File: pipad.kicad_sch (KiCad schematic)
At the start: 2 parts

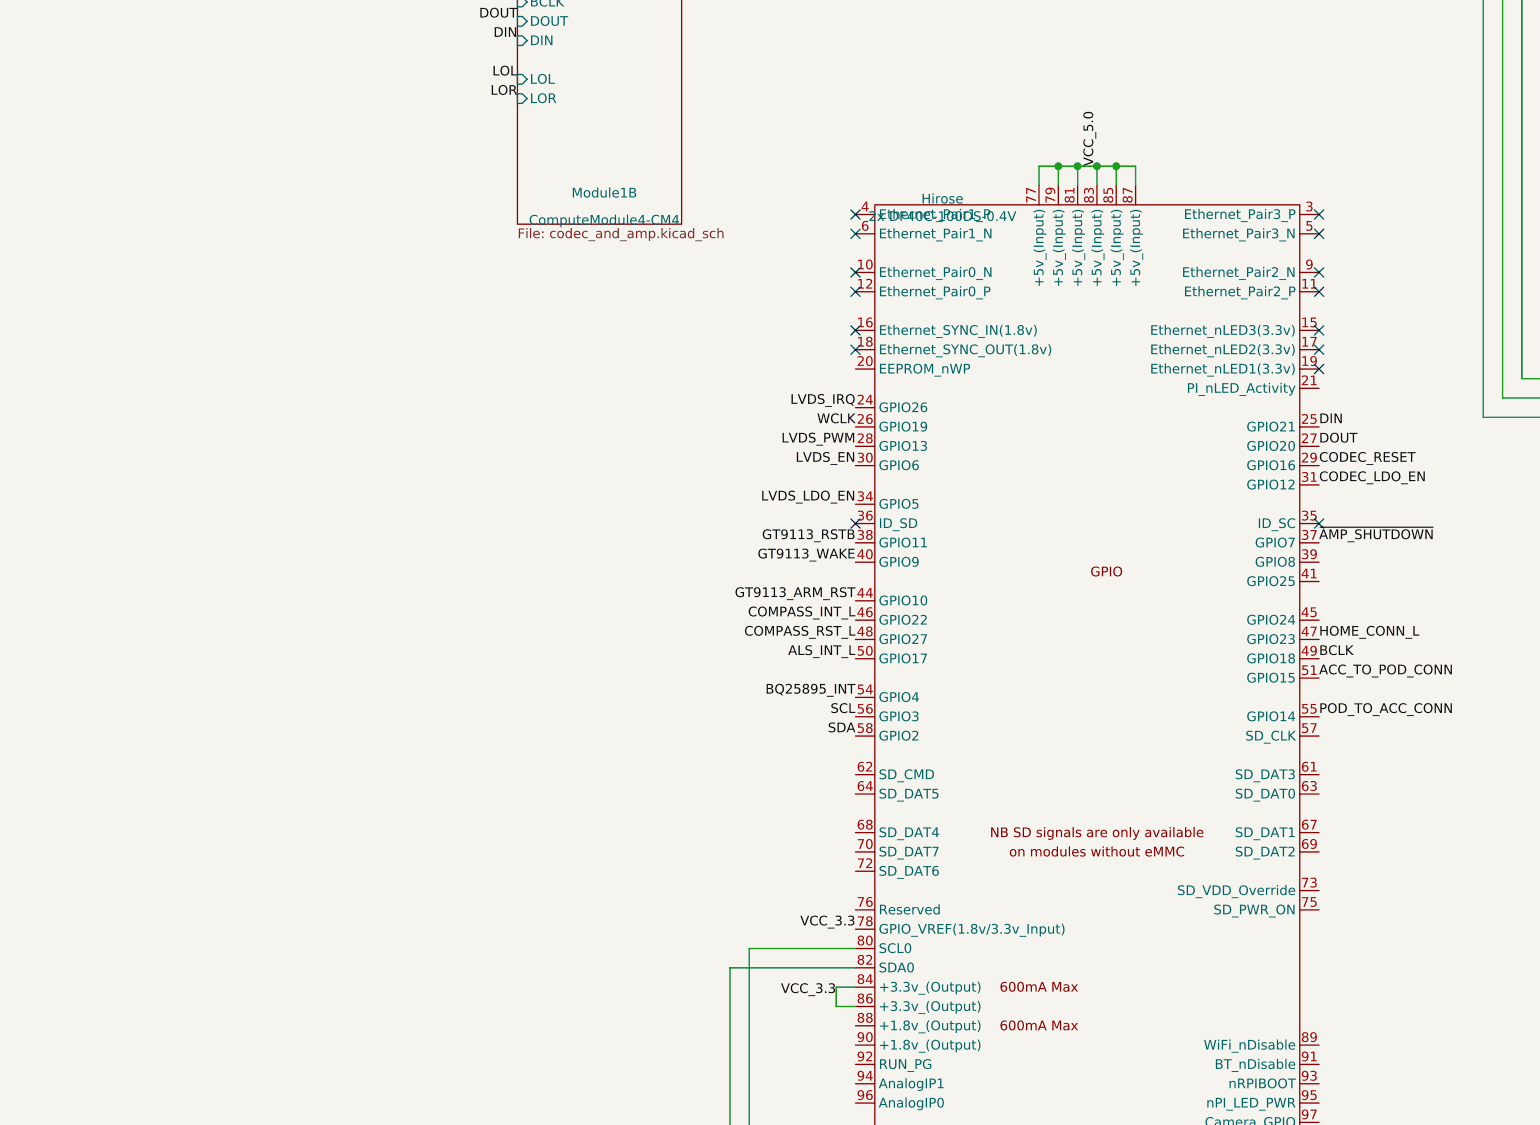
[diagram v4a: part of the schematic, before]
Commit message: Add connector for side buttons; wire up to the last remaining GPIO pins, and wire volume up/down to MFP3/MFP5 pins on the audio codec.
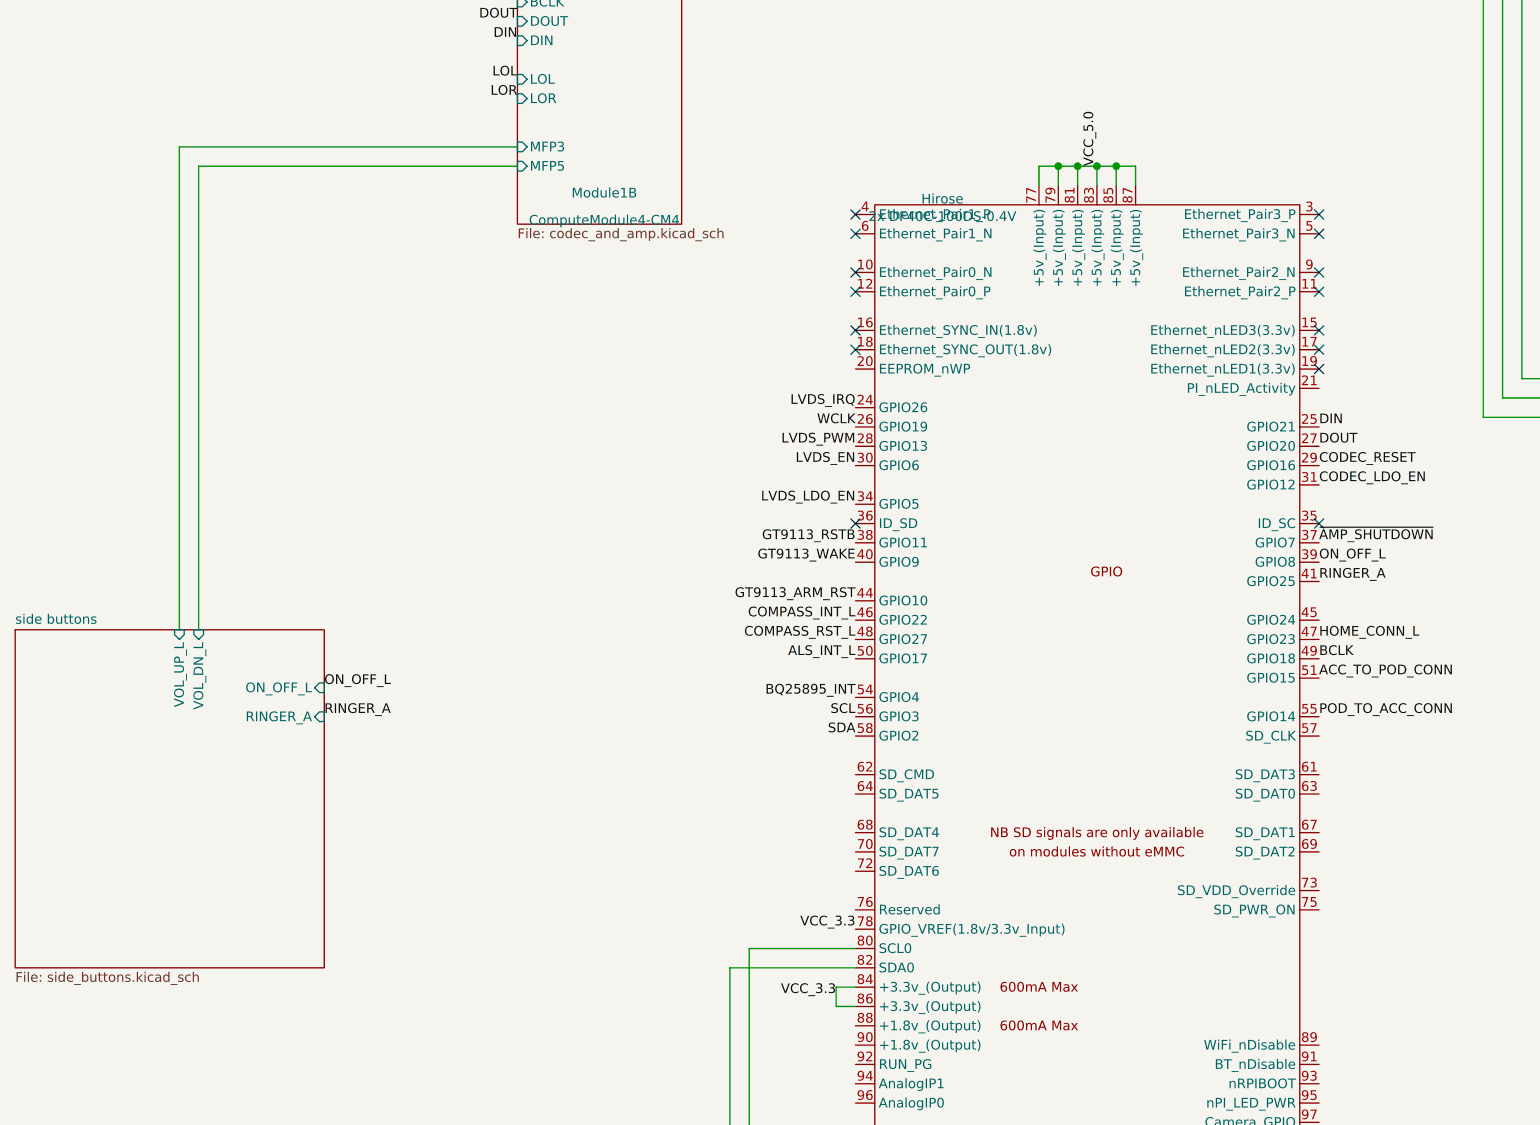
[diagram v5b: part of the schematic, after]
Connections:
- net ON_OFF_L: now reaches Module1.39 (GPIO8)
- net RINGER_A: now reaches Module1.41 (GPIO25)
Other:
- added sheet side buttons (side_buttons.kicad_sch)
- sheet codec and amp ports: added MFP3, MFP5; removed none
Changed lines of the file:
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@@
     (stroke (width 0.1524) (type solid) (color 0 0 0 0))
   )
+  (wire (pts (xy 66.04 139.7) (xy 66.04 203.2))
+    (stroke (width 0) (type solid) (color 0 0 0 0))
+  )
+  (wire (pts (xy 68.58 142.24) (xy 110.49 142.24))
+    (stroke (width 0) (type solid) (color 0 0 0 0))
+  )
+  (wire (pts (xy 68.58 203.2) (xy 68.58 142.24))
+    (stroke (width 0) (type solid) (color 0 0 0 0))
+  )
+  (wire (pts (xy 110.49 139.7) (xy 66.04 139.7))
+    (stroke (width 0) (type solid) (color 0 0 0 0))
+  )
   (wire (pts (xy 138.43 247.65) (xy 138.43 330.2))
     (stroke (width 0) (type solid) (color 0 0 0 0))
@@
     (effects (font (size 1.27 1.27)) (justify left bottom))
   )
+  (label "ON_OFF_L" (at 85.09 210.82 0)
+    (effects (font (size 1.27 1.27)) (justify left bottom))
+  )
+  (label "RINGER_A" (at 85.09 214.63 0)
+    (effects (font (size 1.27 1.27)) (justify left bottom))
+  )
   (label "VCC_3.7" (at 110.49 95.25 180)
     (effects (font (size 1.27 1.27)) (justify right bottom))
@@
   )
   (label "~AMP_SHUTDOWN" (at 215.9 191.77 0)
+    (effects (font (size 1.27 1.27)) (justify left bottom))
+  )
+  (label "ON_OFF_L" (at 215.9 194.31 0)
+    (effects (font (size 1.27 1.27)) (justify left bottom))
+  )
+  (label "RINGER_A" (at 215.9 196.85 0)
     (effects (font (size 1.27 1.27)) (justify left bottom))
   )
@@
       (effects (font (size 1.27 1.27)) (justify left))
     )
+    (pin "MFP3" input (at 110.49 139.7 180)
+      (effects (font (size 1.27 1.27)) (justify left))
+    )
+    (pin "MFP5" input (at 110.49 142.24 180)
+      (effects (font (size 1.27 1.27)) (justify left))
+    )
   )
   (sheet (at 153.67 26.67) (size 36.83 67.31) (fields_autoplaced)
@@
     (pin "RX_P" input (at 269.24 85.09 180)
       (effects (font (size 1.27 1.27)) (justify left))
+    )
+  )
+  (sheet (at 44.45 203.2) (size 40.64 44.45) (fields_autoplaced)
+    (stroke (width 0.0006) (type solid) (color 0 0 0 0))
+    (fill (color 0 0 0 0.0000))
+    (property "Sheet name" "side buttons" (id 0) (at 44.45 202.5643 0)
+      (effects (font (size 1.27 1.27)) (justify left bottom))
+    )
+    (property "Sheet file" "side_buttons.kicad_sch" (id 1) (at 44.45 248.1587 0)
+      (effects (font (size 1.27 1.27)) (justify left top))
+    )
+    (pin "ON_OFF_L" input (at 85.09 210.82 0)
+      (effects (font (size 1.27 1.27)) (justify right))
+    )
+    (pin "RINGER_A" input (at 85.09 214.63 0)
+      (effects (font (size 1.27 1.27)) (justify right))
+    )
+    (pin "VOL_UP_L" input (at 66.04 203.2 90)
+      (effects (font (size 1.27 1.27)) (justify right))
+    )
+    (pin "VOL_DN_L" input (at 68.58 203.2 90)
+      (effects (font (size 1.27 1.27)) (justify right))
     )
   )
@@
     (path "/edc6f2df-f35f-4519-8662-3f6b046c5ebe/" (page "9"))
     (path "/21a15aa6-1f6e-4d00-a58a-2f544b151826/" (page "10"))
+    (path "/0fe5afbd-bd68-4234-ae99-9694af6479f4/" (page "11"))
     (path "/00000000-0000-0000-0000-00006026a3be/e9fc4bb6-5bde-4905-9630-250663643427/" (page " "))
   )
@@
       (reference "J3") (unit 1) (value "pcie_m2_ngff") (footprint "footprints:246411067101894M_and_SM3ZS067U215-NUT1")
     )
+    (path "/0fe5afbd-bd68-4234-ae99-9694af6479f4/07bf0e1f-6cfb-4bb5-bc1a-c9b2e968cc97"
+      (reference "#PWR0144") (unit 1) (value "GND") (footprint "")
+    )
+    (path "/0fe5afbd-bd68-4234-ae99-9694af6479f4/fcf769a8-2162-42a3-a765-47b2346571e4"
+      (reference "J4") (unit 1) (value "Conn_01x08") (footprint "footprints:78171-0006")
+    )
     (path "/00000000-0000-0000-0000-00006026a3be/e9fc4bb6-5bde-4905-9630-250663643427/fd649b90-fe8e-4ecf-a531-c62c874ce18c"

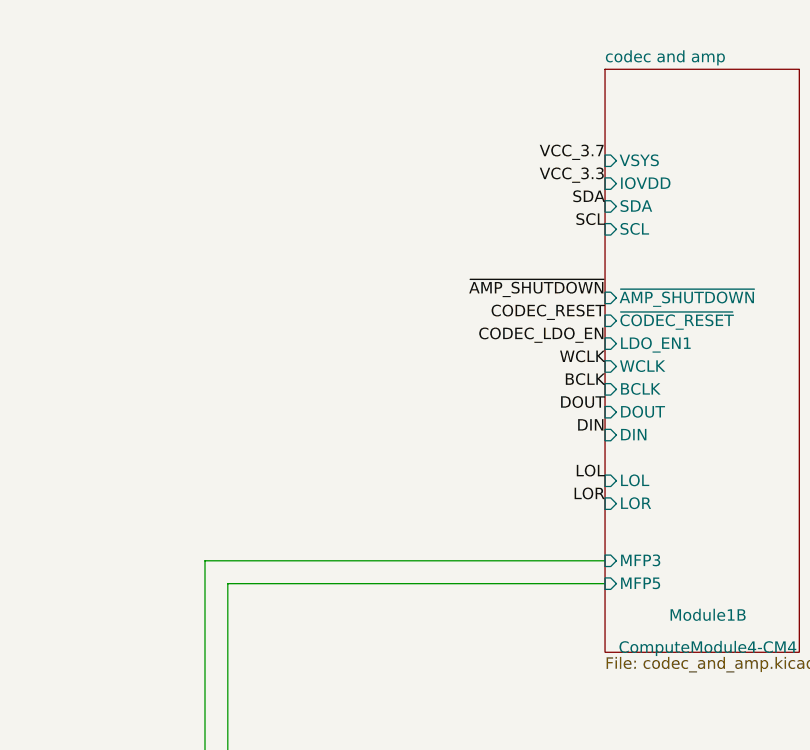
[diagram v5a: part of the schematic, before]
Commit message: Add external pullups for volume up/down buttons
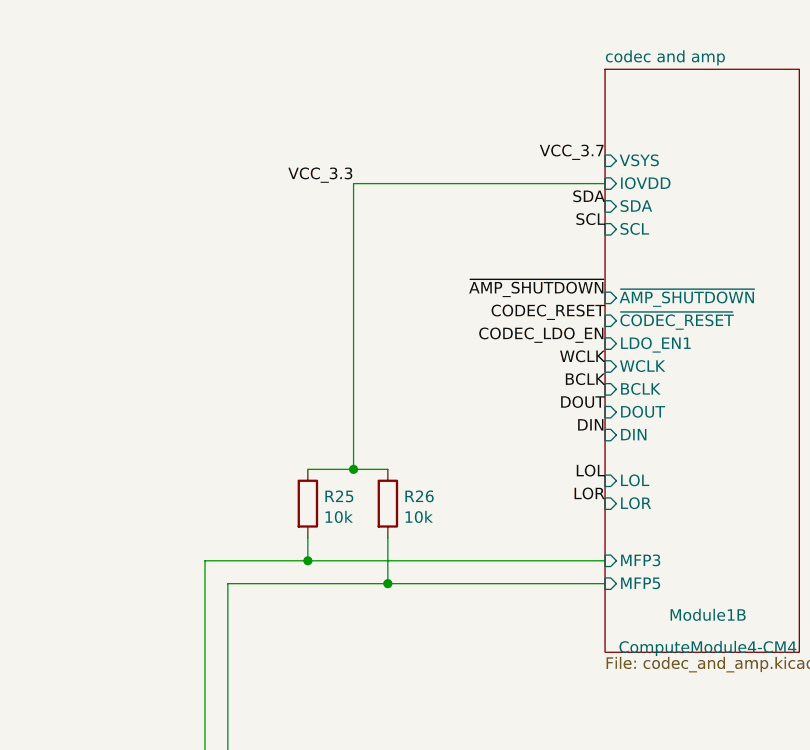
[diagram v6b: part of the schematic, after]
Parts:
- added R25, R26: 10k, Resistor_SMD:R_0402_1005Metric, symbol Device:R
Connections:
- net VCC_3.3: now also R25.1, R26.1
- net codec and amp/MFP3: now also R25.2
- net codec and amp/MFP5: now also R26.2
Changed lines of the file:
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@@
 (kicad_sch (version 20210126) (generator eeschema)
   (paper "C")
+  (junction (at 77.47 139.7) (diameter 1.016) (color 0 0 0 0))
+  (junction (at 82.55 129.54) (diameter 1.016) (color 0 0 0 0))
+  (junction (at 86.36 142.24) (diameter 1.016) (color 0 0 0 0))
   (junction (at 181.61 142.24) (diameter 1.016) (color 0 0 0 0))
   (junction (at 184.15 142.24) (diameter 1.016) (color 0 0 0 0))
@@
     (stroke (width 0) (type solid) (color 0 0 0 0))
   )
-  (wire (pts (xy 68.58 142.24) (xy 110.49 142.24))
+  (wire (pts (xy 66.04 139.7) (xy 77.47 139.7))
+    (stroke (width 0) (type solid) (color 0 0 0 0))
+  )
+  (wire (pts (xy 68.58 142.24) (xy 86.36 142.24))
     (stroke (width 0) (type solid) (color 0 0 0 0))
   )
@@
     (stroke (width 0) (type solid) (color 0 0 0 0))
   )
-  (wire (pts (xy 110.49 139.7) (xy 66.04 139.7))
+  (wire (pts (xy 77.47 129.54) (xy 82.55 129.54))
+    (stroke (width 0) (type solid) (color 0 0 0 0))
+  )
+  (wire (pts (xy 77.47 137.16) (xy 77.47 139.7))
+    (stroke (width 0) (type solid) (color 0 0 0 0))
+  )
+  (wire (pts (xy 77.47 139.7) (xy 110.49 139.7))
+    (stroke (width 0) (type solid) (color 0 0 0 0))
+  )
+  (wire (pts (xy 82.55 97.79) (xy 82.55 129.54))
+    (stroke (width 0) (type solid) (color 0 0 0 0))
+  )
+  (wire (pts (xy 82.55 97.79) (xy 110.49 97.79))
+    (stroke (width 0) (type solid) (color 0 0 0 0))
+  )
+  (wire (pts (xy 82.55 129.54) (xy 86.36 129.54))
+    (stroke (width 0) (type solid) (color 0 0 0 0))
+  )
+  (wire (pts (xy 86.36 137.16) (xy 86.36 142.24))
+    (stroke (width 0) (type solid) (color 0 0 0 0))
+  )
+  (wire (pts (xy 86.36 142.24) (xy 110.49 142.24))
     (stroke (width 0) (type solid) (color 0 0 0 0))
   )
@@
     (effects (font (size 1.27 1.27)) (justify left bottom))
   )
+  (label "VCC_3.3" (at 82.55 97.79 180)
+    (effects (font (size 1.27 1.27)) (justify right bottom))
+  )
   (label "ON_OFF_L" (at 85.09 210.82 0)
     (effects (font (size 1.27 1.27)) (justify left bottom))
@@
   )
   (label "VCC_3.7" (at 110.49 95.25 180)
-    (effects (font (size 1.27 1.27)) (justify right bottom))
-  )
-  (label "VCC_3.3" (at 110.49 97.79 180)
     (effects (font (size 1.27 1.27)) (justify right bottom))
   )
@@
     )
     (pin "1")
+  )
+  (symbol (lib_id "Device:R") (at 77.47 133.35 0) (unit 1)
+    (in_bom yes) (on_board yes) (fields_autoplaced)
+    (property "Reference" "R25" (id 0) (at 79.2481 132.5891 0)
+      (effects (font (size 1.27 1.27)) (justify left))
+    )
+    (property "Value" "10k" (id 1) (at 79.2481 134.8878 0)
+      (effects (font (size 1.27 1.27)) (justify left))
+    )
+    (property "Footprint" "Resistor_SMD:R_0402_1005Metric" (id 2) (at 75.692 133.35 90)
+      (effects (font (size 1.27 1.27)) hide)
+    )
+    (property "Datasheet" "~" (id 3) (at 77.47 133.35 0)
+      (effects (font (size 1.27 1.27)) hide)
+    )
+    (pin "1")
+    (pin "2")
+  )
+  (symbol (lib_id "Device:R") (at 86.36 133.35 0) (unit 1)
+    (in_bom yes) (on_board yes) (fields_autoplaced)
+    (property "Reference" "R26" (id 0) (at 88.1381 132.5891 0)
+      (effects (font (size 1.27 1.27)) (justify left))
+    )
+    (property "Value" "10k" (id 1) (at 88.1381 134.8878 0)
+      (effects (font (size 1.27 1.27)) (justify left))
+    )
+    (property "Footprint" "Resistor_SMD:R_0402_1005Metric" (id 2) (at 84.582 133.35 90)
+      (effects (font (size 1.27 1.27)) hide)
+    )
+    (property "Datasheet" "~" (id 3) (at 86.36 133.35 0)
+      (effects (font (size 1.27 1.27)) hide)
+    )
+    (pin "1")
+    (pin "2")
   )
   (symbol (lib_name "CM4IO:ComputeModule4-CM4_1") (lib_id "CM4IO:ComputeModule4-CM4") (at 147.32 207.01 0) (unit 2)
@@
       (reference "Module1") (unit 2) (value "ComputeModule4-CM4") (footprint "footprints:Raspberry-Pi-4-Compute-Module")
     )
+    (path "/6a461c4f-445b-42e9-8487-fec41d772a0d"
+      (reference "R25") (unit 1) (value "10k") (footprint "Resistor_SMD:R_0402_1005Metric")
+    )
+    (path "/df5408ae-4e5a-4054-aba4-cb01887ffdb5"
+      (reference "R26") (unit 1) (value "10k") (footprint "Resistor_SMD:R_0402_1005Metric")
+    )
     (path "/ffb64783-aa4c-484c-887c-79ad41f72096"

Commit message: Add datasheet for MP3422 boost converter
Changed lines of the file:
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@@
     (effects (font (size 1.27 1.27)) (justify left bottom))
-  )
-  (label "VCC_3.3" (at 82.55 97.79 180)
-    (effects (font (size 1.27 1.27)) (justify right bottom))
   )
   (label "ON_OFF_L" (at 85.09 210.82 0)
@@
     (effects (font (size 1.27 1.27)) (justify right bottom))
   )
+  (label "VCC_3.3" (at 110.49 97.79 180)
+    (effects (font (size 1.27 1.27)) (justify right bottom))
+  )
